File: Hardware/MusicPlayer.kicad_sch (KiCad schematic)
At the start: 32 parts, among them J1 USB_B_Micro, J2 AudioJack3, SW1 SW_Nidec_CAS-120A1, SW2 SW_Nidec_CAS-120A1, U1 MICROSD_SPI_OR_SDIO_CARD, U2 AMS1117, U3 ESP32-S3-WROOM-1, U4 TPS61090

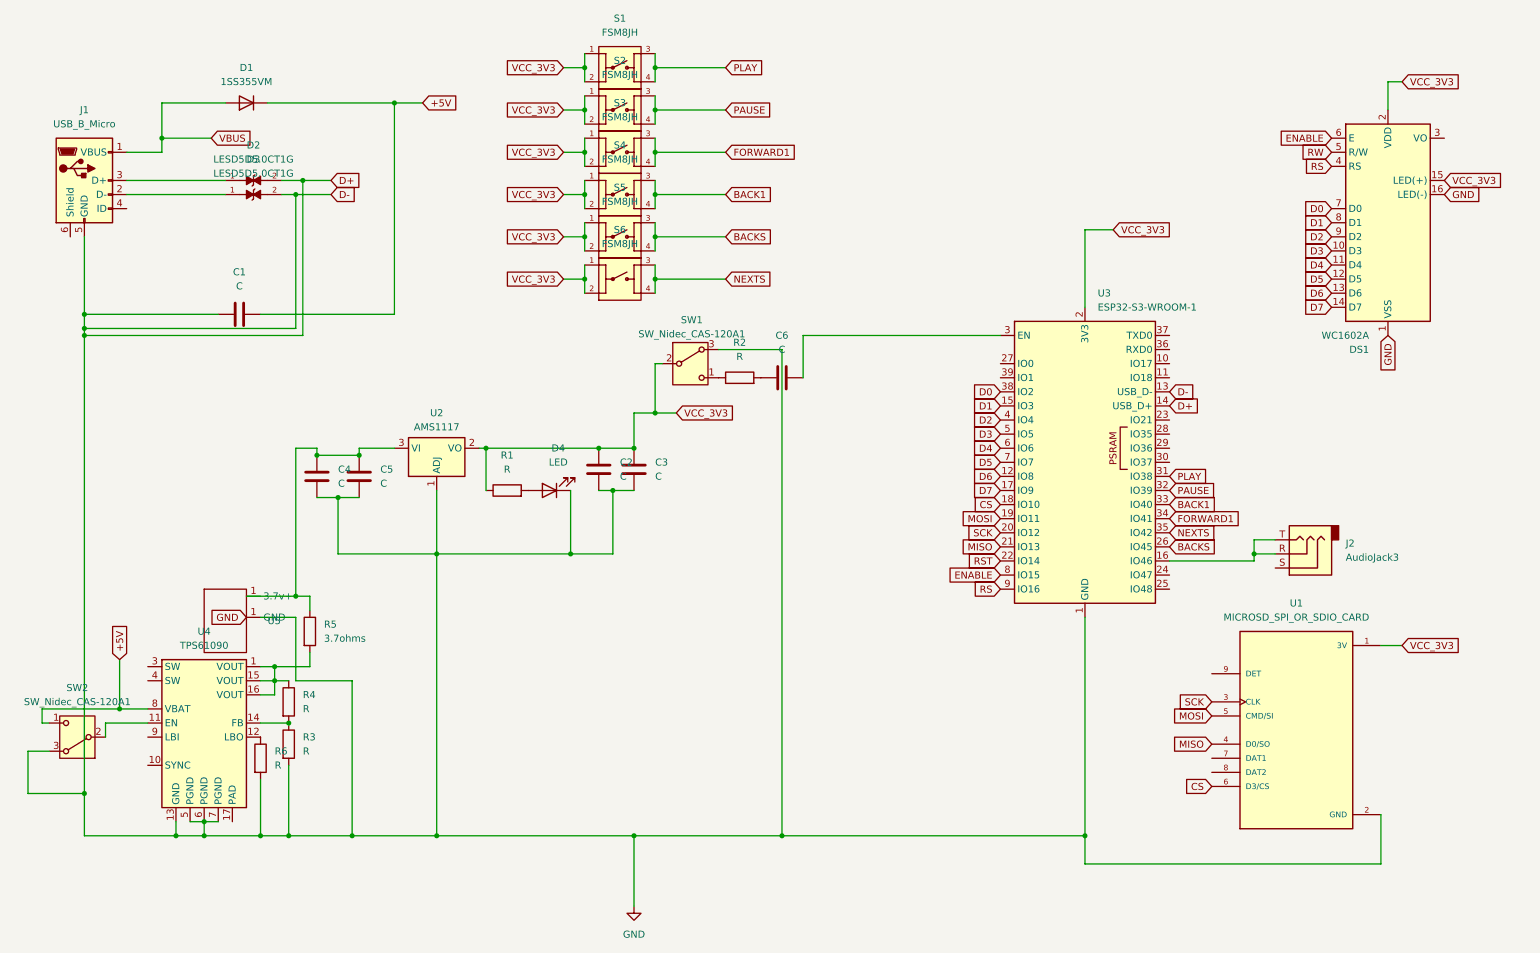
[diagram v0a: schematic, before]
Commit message: added the button control + volume control
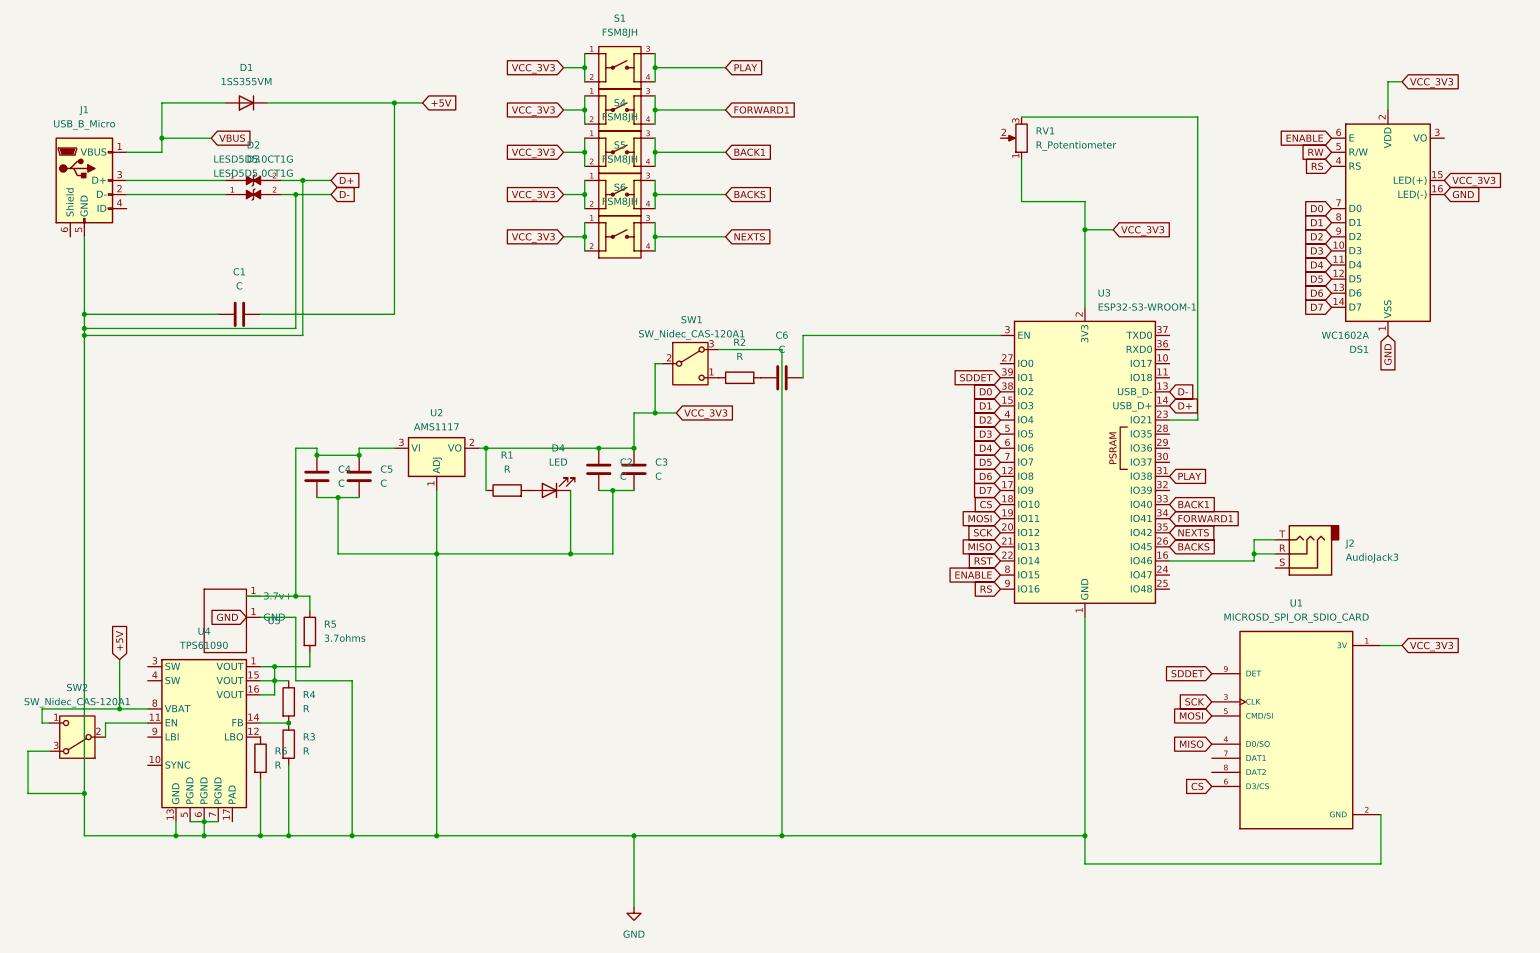
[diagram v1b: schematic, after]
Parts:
- removed S2: FSM8JH, FSM8JH:SW_FSM8JH, symbol FSM8JH:FSM8JH
- added RV1: R_Potentiometer, Potentiometer_SMD:Potentiometer_Bourns_3314S_Horizontal, symbol Device:R_Potentiometer
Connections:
- net VCC_3V3: now also RV1.1
- net SDDET: now reaches U1.9 (DET)
- net SDDET: now also U3.39 (IO1)
- net at U3.23 (IO21): now also RV1.3
- net PAUSE: no longer names the net of U3.32 (IO39)
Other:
- moved on the sheet: S4, S5, S6

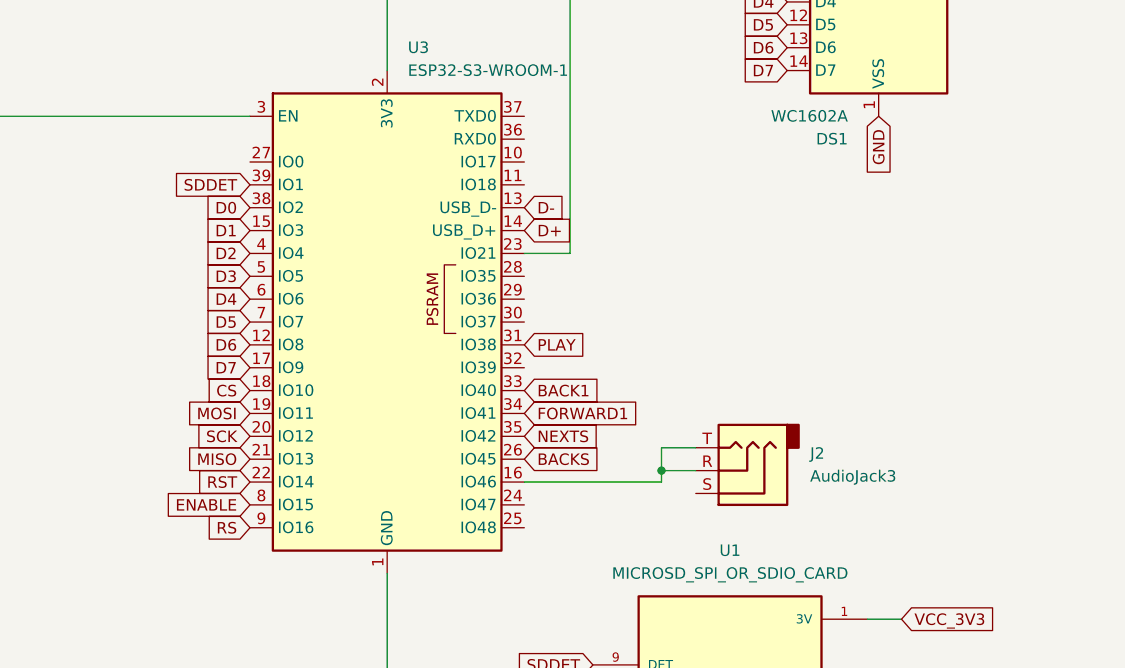
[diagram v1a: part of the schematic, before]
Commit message: bux fixed and updated the schematic with a DAC for sound output
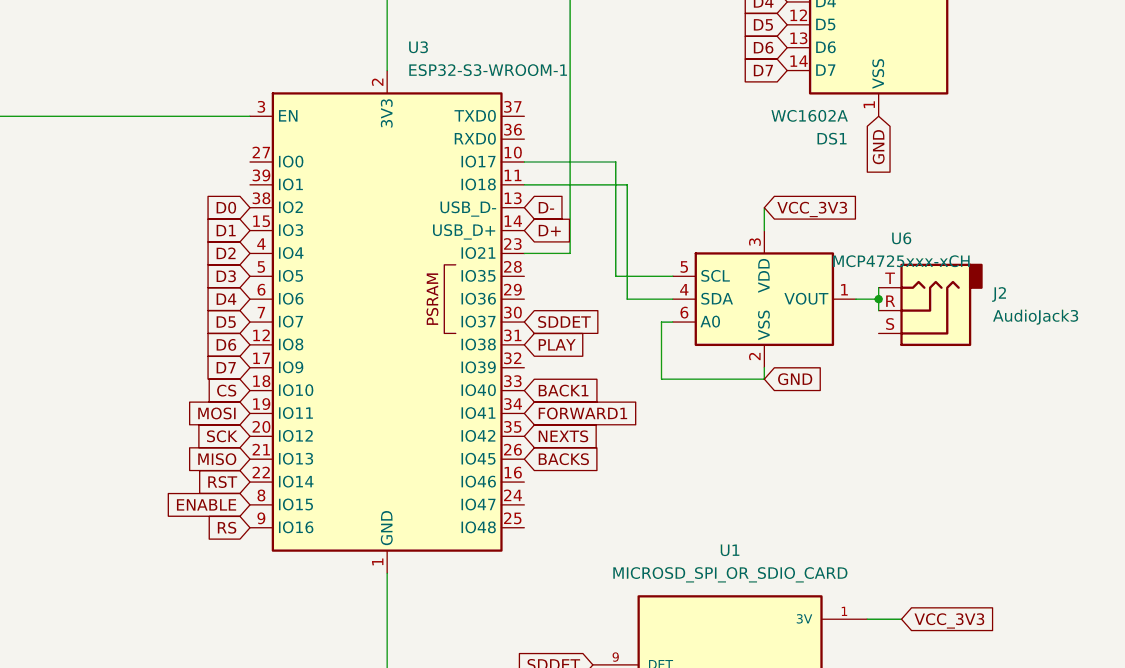
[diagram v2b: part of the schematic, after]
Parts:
- added U6: MCP4725xxx-xCH, Package_TO_SOT_SMD:SOT-23-6, symbol Analog_DAC:MCP4725xxx-xCH
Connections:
- net GND: now also U6.2 (VSS), U6.6 (A0)
- net SDDET: now also U3.30 (IO37); no longer U3.39 (IO1)
- net VCC_3V3: now also U6.3 (VDD)
- net at J2.R, J2.T: now also U6.1 (VOUT); no longer U3.16 (IO46)
- net at U3.10 (IO17): now also U6.5 (SCL)
- net at U3.11 (IO18): now also U6.4 (SDA)
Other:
- moved on the sheet: J2
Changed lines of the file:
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@@
 	)
 	(junction
+		(at 260.35 87.63)
+		(diameter 0)
+		(color 0 0 0 0)
+	)
+	(junction
 		(at 25.4 66.04)
 		(diameter 0)
@@
 	)
 	(junction
-		(at 236.22 106.68)
-		(diameter 0)
-		(color 0 0 0 0)
-	)
-	(junction
 		(at 62.23 157.48)
 		(diameter 0)
@@
 	(wire
 		(pts
-			(xy 33.02 34.29) (xy 39.37 34.29)
+			(xy 247.65 96.52) (xy 247.65 95.25)
 		)
 		(stroke
@@
 	(wire
 		(pts
-			(xy 236.22 104.14) (xy 240.03 104.14)
+			(xy 33.02 34.29) (xy 39.37 34.29)
 		)
 		(stroke
@@
 	(wire
 		(pts
+			(xy 236.22 90.17) (xy 237.49 90.17)
+		)
+		(stroke
+			(width 0)
+			(type default)
+		)
+	)
+	(wire
+		(pts
 			(xy 205.74 118.11) (xy 205.74 157.48)
 		)
@@
 	(wire
 		(pts
-			(xy 124.46 157.48) (xy 151.13 157.48)
+			(xy 231.14 72.39) (xy 231.14 85.09)
 		)
 		(stroke
@@
 	(wire
 		(pts
-			(xy 67.31 87.63) (xy 67.31 88.9)
+			(xy 232.41 87.63) (xy 237.49 87.63)
 		)
 		(stroke
@@
 	(wire
 		(pts
-			(xy 262.89 123.19) (xy 259.08 123.19)
+			(xy 124.46 157.48) (xy 151.13 157.48)
 		)
 		(stroke
@@
 	(wire
 		(pts
-			(xy 64.77 39.37) (xy 69.85 39.37)
+			(xy 67.31 87.63) (xy 67.31 88.9)
 		)
 		(stroke
@@
 	(wire
 		(pts
-			(xy 63.5 87.63) (xy 63.5 114.3)
+			(xy 262.89 123.19) (xy 259.08 123.19)
 		)
 		(stroke
@@
 	(wire
 		(pts
-			(xy 115.57 24.13) (xy 115.57 26.67)
+			(xy 64.77 39.37) (xy 69.85 39.37)
+		)
+		(stroke
+			(width 0)
+			(type default)
+		)
+	)
+	(wire
+		(pts
+			(xy 63.5 87.63) (xy 63.5 114.3)
 		)
 		(stroke
@@
 	(wire
 		(pts
-			(xy 240.03 106.68) (xy 236.22 106.68)
+			(xy 115.57 24.13) (xy 115.57 26.67)
 		)
 		(stroke
@@
 	(wire
 		(pts
+			(xy 257.81 87.63) (xy 260.35 87.63)
+		)
+		(stroke
+			(width 0)
+			(type default)
+		)
+	)
+	(wire
+		(pts
 			(xy 36.83 137.16) (xy 29.21 137.16)
 		)
@@
 	(wire
 		(pts
+			(xy 231.14 85.09) (xy 237.49 85.09)
+		)
+		(stroke
+			(width 0)
+			(type default)
+		)
+	)
+	(wire
+		(pts
+			(xy 220.98 72.39) (xy 231.14 72.39)
+		)
+		(stroke
+			(width 0)
+			(type default)
+		)
+	)
+	(wire
+		(pts
 			(xy 124.46 170.18) (xy 124.46 157.48)
 		)
@@
 	(wire
 		(pts
-			(xy 236.22 107.95) (xy 236.22 106.68)
+			(xy 128.27 19.05) (xy 140.97 19.05)
 		)
 		(stroke
@@
 	(wire
 		(pts
-			(xy 128.27 19.05) (xy 140.97 19.05)
+			(xy 63.5 118.11) (xy 63.5 129.54)
 		)
 		(stroke
@@
 	(wire
 		(pts
-			(xy 63.5 118.11) (xy 63.5 129.54)
+			(xy 260.35 86.36) (xy 260.35 87.63)
 		)
 		(stroke
@@
 	(wire
 		(pts
+			(xy 260.35 87.63) (xy 260.35 88.9)
+		)
+		(stroke
+			(width 0)
+			(type default)
+		)
+	)
+	(wire
+		(pts
 			(xy 210.82 48.26) (xy 205.74 48.26)
 		)
@@
 	(wire
 		(pts
+			(xy 236.22 96.52) (xy 247.65 96.52)
+		)
+		(stroke
+			(width 0)
+			(type default)
+		)
+	)
+	(wire
+		(pts
 			(xy 205.74 48.26) (xy 205.74 62.23)
 		)
@@
 	(wire
 		(pts
-			(xy 236.22 106.68) (xy 236.22 104.14)
-		)
-		(stroke
-			(width 0)
-			(type default)
-		)
-	)
-	(wire
-		(pts
 			(xy 194.31 27.94) (xy 226.06 27.94)
 		)
@@
 	(wire
 		(pts
+			(xy 247.65 77.47) (xy 247.65 80.01)
+		)
+		(stroke
+			(width 0)
+			(type default)
+		)
+	)
+	(wire
+		(pts
 			(xy 67.31 88.9) (xy 74.93 88.9)
 		)
@@
 	(wire
 		(pts
-			(xy 220.98 107.95) (xy 236.22 107.95)
-		)
-		(stroke
-			(width 0)
-			(type default)
-		)
-	)
-	(wire
-		(pts
 			(xy 151.13 157.48) (xy 205.74 157.48)
 		)
@@
 	(wire
 		(pts
+			(xy 220.98 74.93) (xy 232.41 74.93)
+		)
+		(stroke
+			(width 0)
+			(type default)
+		)
+	)
+	(wire
+		(pts
 			(xy 128.27 34.29) (xy 140.97 34.29)
 		)
@@
 	(wire
 		(pts
+			(xy 232.41 74.93) (xy 232.41 87.63)
+		)
+		(stroke
+			(width 0)
+			(type default)
+		)
+	)
+	(wire
+		(pts
 			(xy 194.31 35.56) (xy 194.31 43.18)
 		)
@@
 	(wire
 		(pts
+			(xy 236.22 90.17) (xy 236.22 96.52)
+		)
+		(stroke
+			(width 0)
+			(type default)
+		)
+	)
+	(wire
+		(pts
 			(xy 128.27 19.05) (xy 128.27 21.59)
 		)
@@
 		)
 	)
+	(global_label "GND"
+		(shape input)
+		(at 247.65 96.52 0)
+		(fields_autoplaced yes)
+		(effects
+			(font
+				(size 1.27 1.27)
+			)
+			(justify left)
+		)
+		(property "Intersheetrefs" "${INTERSHEET_REFS}"
+			(at 254.2343 96.52 0)
+			(effects
+				(font
+					(size 1.27 1.27)
+				)
+				(justify left)
+				(hide yes)
+			)
+		)
+	)
 	(global_label "MISO"
 		(shape input)
@@
 		)
 	)
+	(global_label "VCC_3V3"
+		(shape input)
+		(at 247.65 77.47 0)
+		(fields_autoplaced yes)
+		(effects
+			(font
+				(size 1.27 1.27)
+			)
+			(justify left)
+		)
+		(property "Intersheetrefs" "${INTERSHEET_REFS}"
+			(at 257.5161 77.47 0)
+			(effects
+				(font
+					(size 1.27 1.27)
+				)
+				(justify left)
+				(hide yes)
+			)
+		)
+	)
 	(global_label "FORWARD1"
 		(shape input)
@@
 	(global_label "SDDET"
 		(shape input)
-		(at 190.5 74.93 180)
+		(at 220.98 90.17 0)
 		(fields_autoplaced yes)
 		(effects
@@
 				(size 1.27 1.27)
 			)
-			(justify right)
+			(justify left)
 		)
 		(property "Intersheetrefs" "${INTERSHEET_REFS}"
-			(at 182.4008 74.93 0)
+			(at 229.0792 90.17 0)
 			(effects
 				(font
 					(size 1.27 1.27)
 				)
-				(justify right)
+				(justify left)
 				(hide yes)
 			)
@@
 	)
 	(symbol
+		(lib_id "Analog_DAC:MCP4725xxx-xCH")
+		(at 247.65 87.63 0)
+		(unit 1)
+		(exclude_from_sim no)
+		(in_bom yes)
+		(on_board yes)
+		(dnp no)
+		(fields_autoplaced yes)
+		(property "Reference" "U6"
+			(at 262.89 80.9215 0)
+			(effects
+				(font
+					(size 1.27 1.27)
+				)
+			)
+		)
+		(property "Value" "MCP4725xxx-xCH"
+			(at 262.89 83.4615 0)
+			(effects
+				(font
+					(size 1.27 1.27)
+				)
+			)
+		)
+		(property "Footprint" "Package_TO_SOT_SMD:SOT-23-6"
+			(at 247.65 93.98 0)
+			(effects
+				(font
+					(size 1.27 1.27)
+				)
+				(hide yes)
+			)
+		)
+		(property "Datasheet" "http://ww1.microchip.com/downloads/en/DeviceDoc/22039d.pdf"
+			(at 247.65 87.63 0)
+			(effects
+				(font
+					(size 1.27 1.27)
+				)
+				(hide yes)
+			)
+		)
+		(property "Description" "12-bit Digital-to-Analog Converter, integrated EEPROM, I2C interface, SOT-23-6"
+			(at 247.65 87.63 0)
+			(effects
+				(font
+					(size 1.27 1.27)
+				)
+				(hide yes)
+			)
+		)
+		(pin "6"
+		)
+		(pin "2"
+		)
+		(pin "1"
+		)
+		(pin "4"
+		)
+		(pin "3"
+		)
+		(pin "5"
+		)
+		(instances
+			(project ""
+				(path "/2b7a1a48-2553-49e3-90ba-0bcdb9a91407"
+					(reference "U6")
+					(unit 1)
+				)
+			)
+		)
+	)
+	(symbol
 		(lib_id "FSM8JH:FSM8JH")
 		(at 121.92 49.53 0)
@@
 	(symbol
 		(lib_id "Connector_Audio:AudioJack3")
-		(at 245.11 106.68 180)
+		(at 265.43 88.9 180)
 		(unit 1)
 		(exclude_from_sim no)
@@
 		(fields_autoplaced yes)
 		(property "Reference" "J2"
-			(at 252.73 104.775 0)
+			(at 273.05 86.995 0)
 			(effects
 				(font
@@
 		)
 		(property "Value" "AudioJack3"
-			(at 252.73 107.315 0)
+			(at 273.05 89.535 0)
 			(effects
 				(font
@@
 		)
 		(property "Footprint" "Connector_Audio:Jack_3.5mm_CUI_SJ-3523-SMT_Horizontal"
-			(at 245.11 106.68 0)
+			(at 265.43 88.9 0)
 			(effects
 				(font
@@
 		)
 		(property "Datasheet" "~"
-			(at 245.11 106.68 0)
+			(at 265.43 88.9 0)
 			(effects
 				(font
@@
 		)
 		(property "Description" "Audio Jack, 3 Poles (Stereo / TRS)"
-			(at 245.11 106.68 0)
+			(at 265.43 88.9 0)
 			(effects
 				(font
